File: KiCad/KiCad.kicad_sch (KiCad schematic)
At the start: 0 parts

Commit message: 提交初始BOM表
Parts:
- added U1: ESP32-WROOM-32E, RF_Module:ESP32-WROOM-32D, symbol RF_Module:ESP32-WROOM-32E
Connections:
- new net +3V3: U1.2 (VDD)
- new net GND: U1.1 (GND), U1.15 (GND), U1.38 (GND), U1.39 (GND)
- no-connect marks 0 -> 1

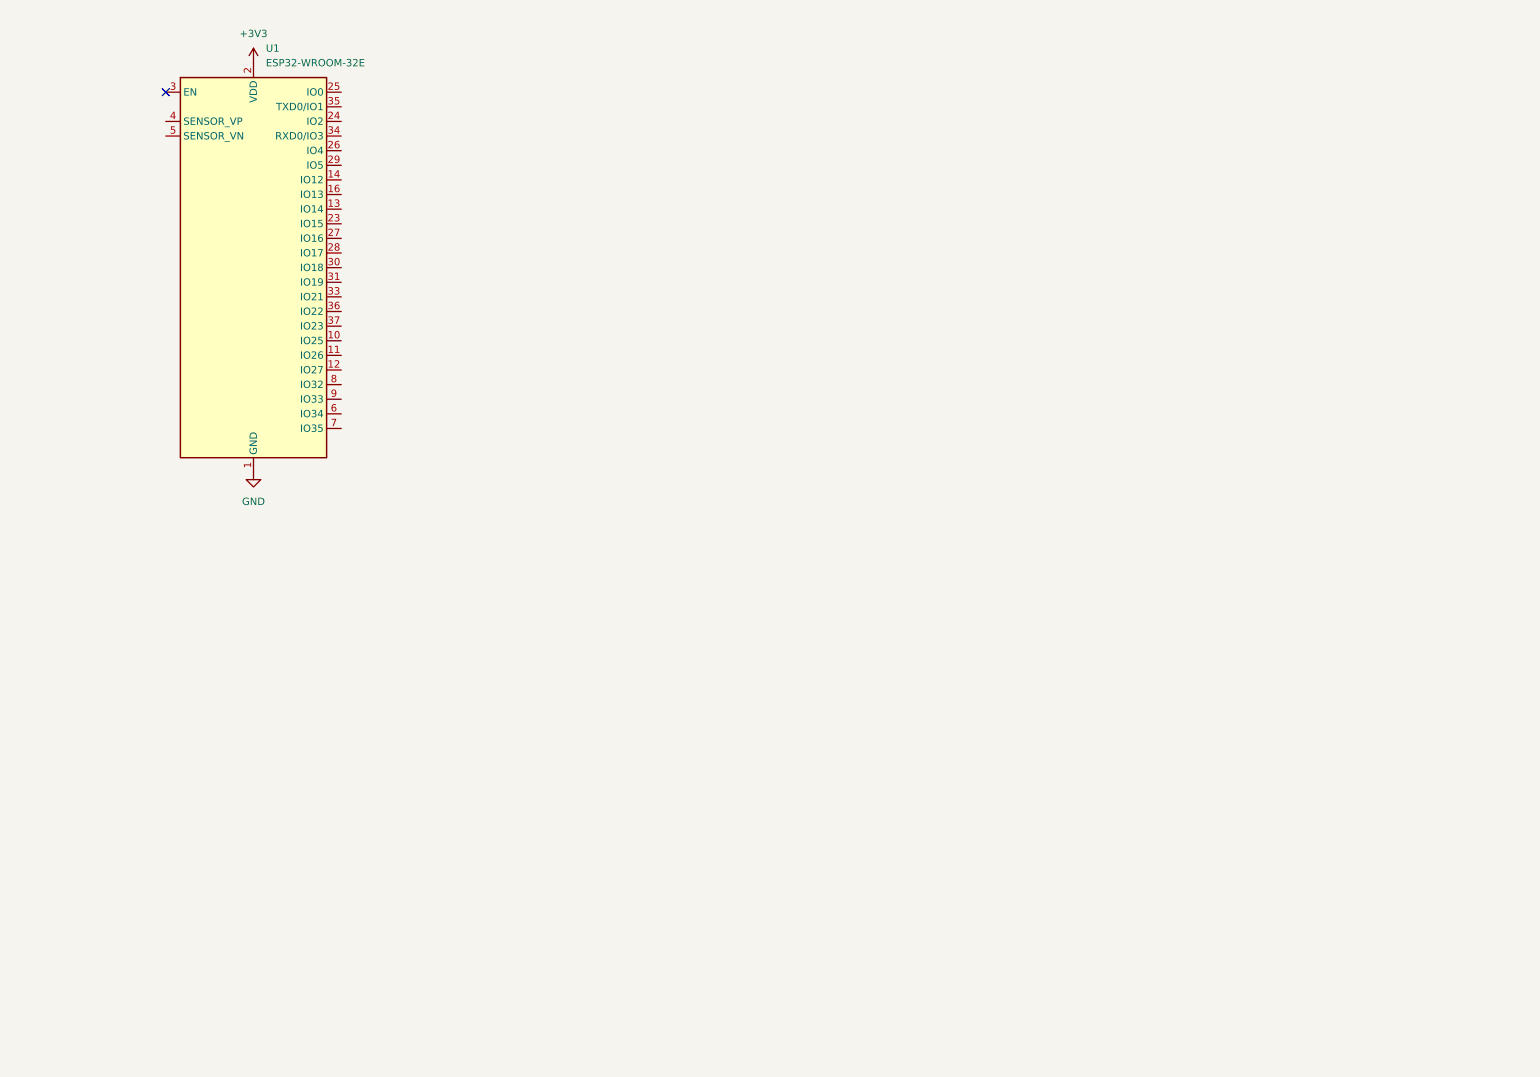
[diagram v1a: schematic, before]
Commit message: 完成主電源輸入轉到數位系統主電源軌電壓(12~24v to 5v)之原理圖，包含外部DC供電接口
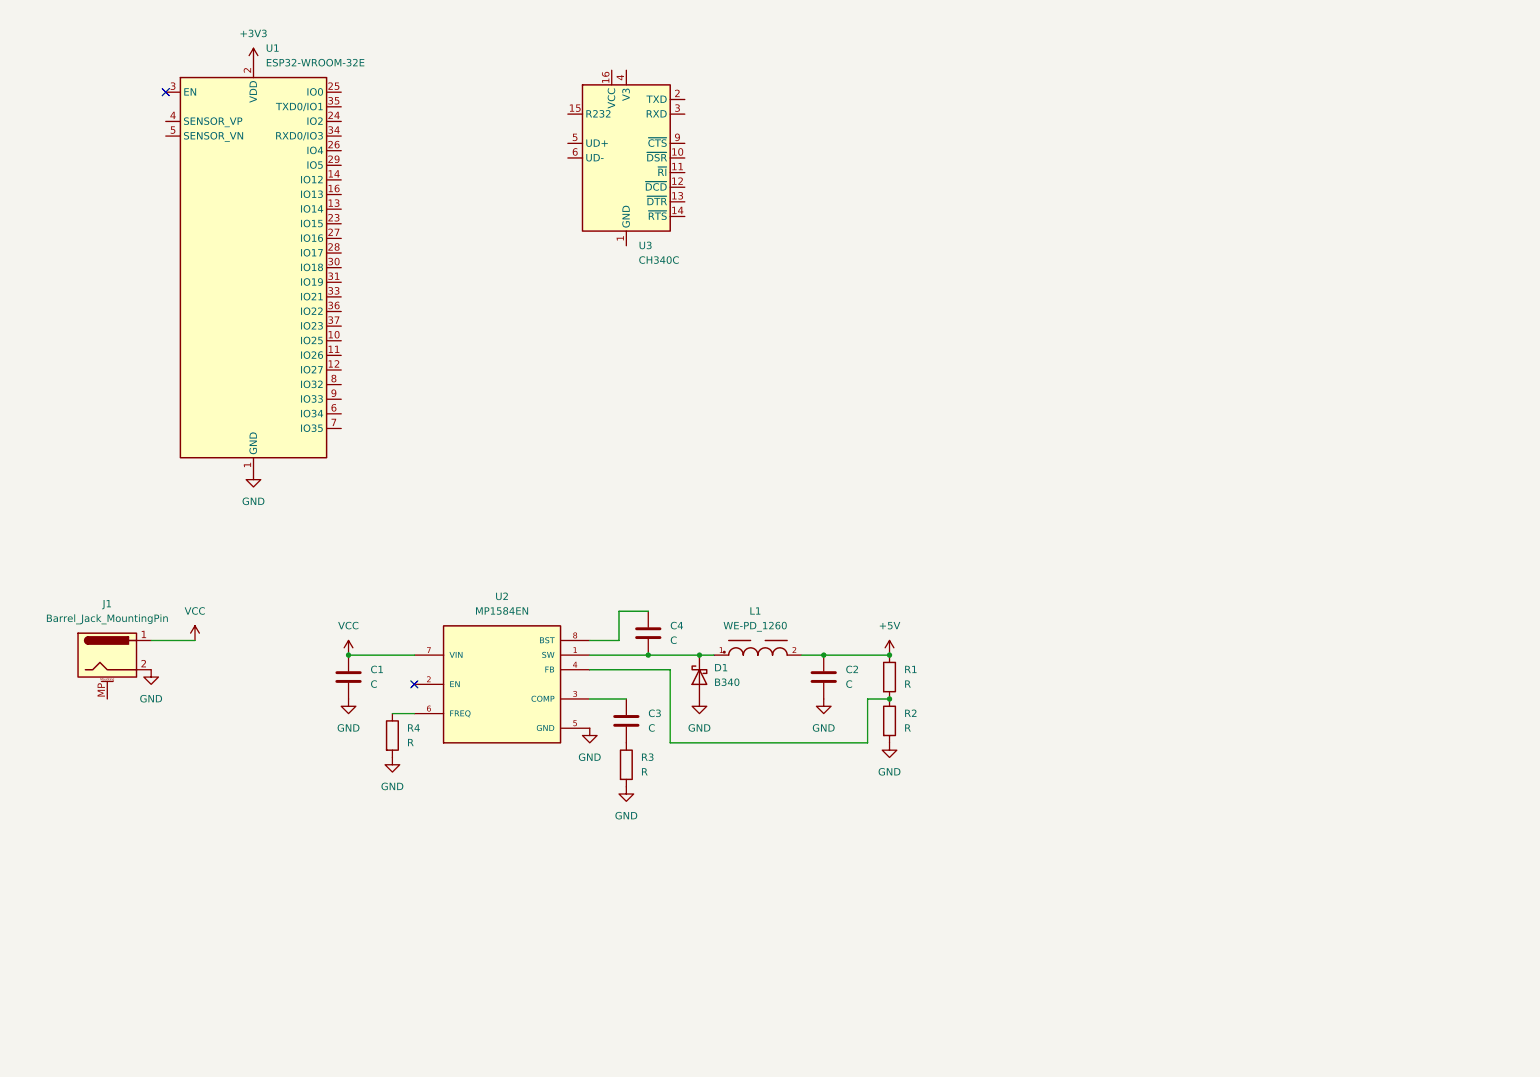
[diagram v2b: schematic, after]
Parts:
- added C1, C2, C3, C4: C, Capacitor_SMD:C_0603_1608Metric, symbol Device:C
- added D1: B340, Diode_SMD:D_SMC, symbol Diode:B340
- added J1: Barrel_Jack_MountingPin, Connector_BarrelJack:BarrelJack_Kycon_KLDX-0202-xC_Horizontal, symbol Connector:Barrel_Jack_MountingPin
- added L1: WE-PD_1260, DC-DC POWER L1:WE-PD_1260, symbol DC-DC POWER L1:WE-PD_1260
- added R1, R2, R4: R, Resistor_SMD:R_0603_1608Metric, symbol Device:R
- added R3: R, symbol Device:R
- added U2: MP1584EN, MP1584:SOIC127P600X170-9N, symbol MP1584:MP1584EN
- added U3: CH340C, Package_SO:SOIC-16_3.9x9.9mm_P1.27mm, symbol Interface_USB:CH340C
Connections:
- net GND: now also C1.2, C2.2, D1.2 (A), J1.2, R2.2, R3.2, R4.2, U2.5 (GND), U2.9 (GND)
- new net: R1.2, R2.1, U2.4 (FB)
- new net: C4.2, D1.1 (K), L1.1, U2.1 (SW)
- new net: C3.1, U2.3 (COMP)
- new net: R4.1, U2.6 (FREQ)
- new net: C4.1, U2.8 (BST)
- new net: C3.2, R3.1
- new net +5V: C2.1, L1.2, R1.1
- new net VCC: C1.1, J1.1, U2.7 (VIN)
- no-connect marks 1 -> 2

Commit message: 完成主電源輸入轉到數位系統主電源軌電壓模塊(12~24v to 5v)之PCB
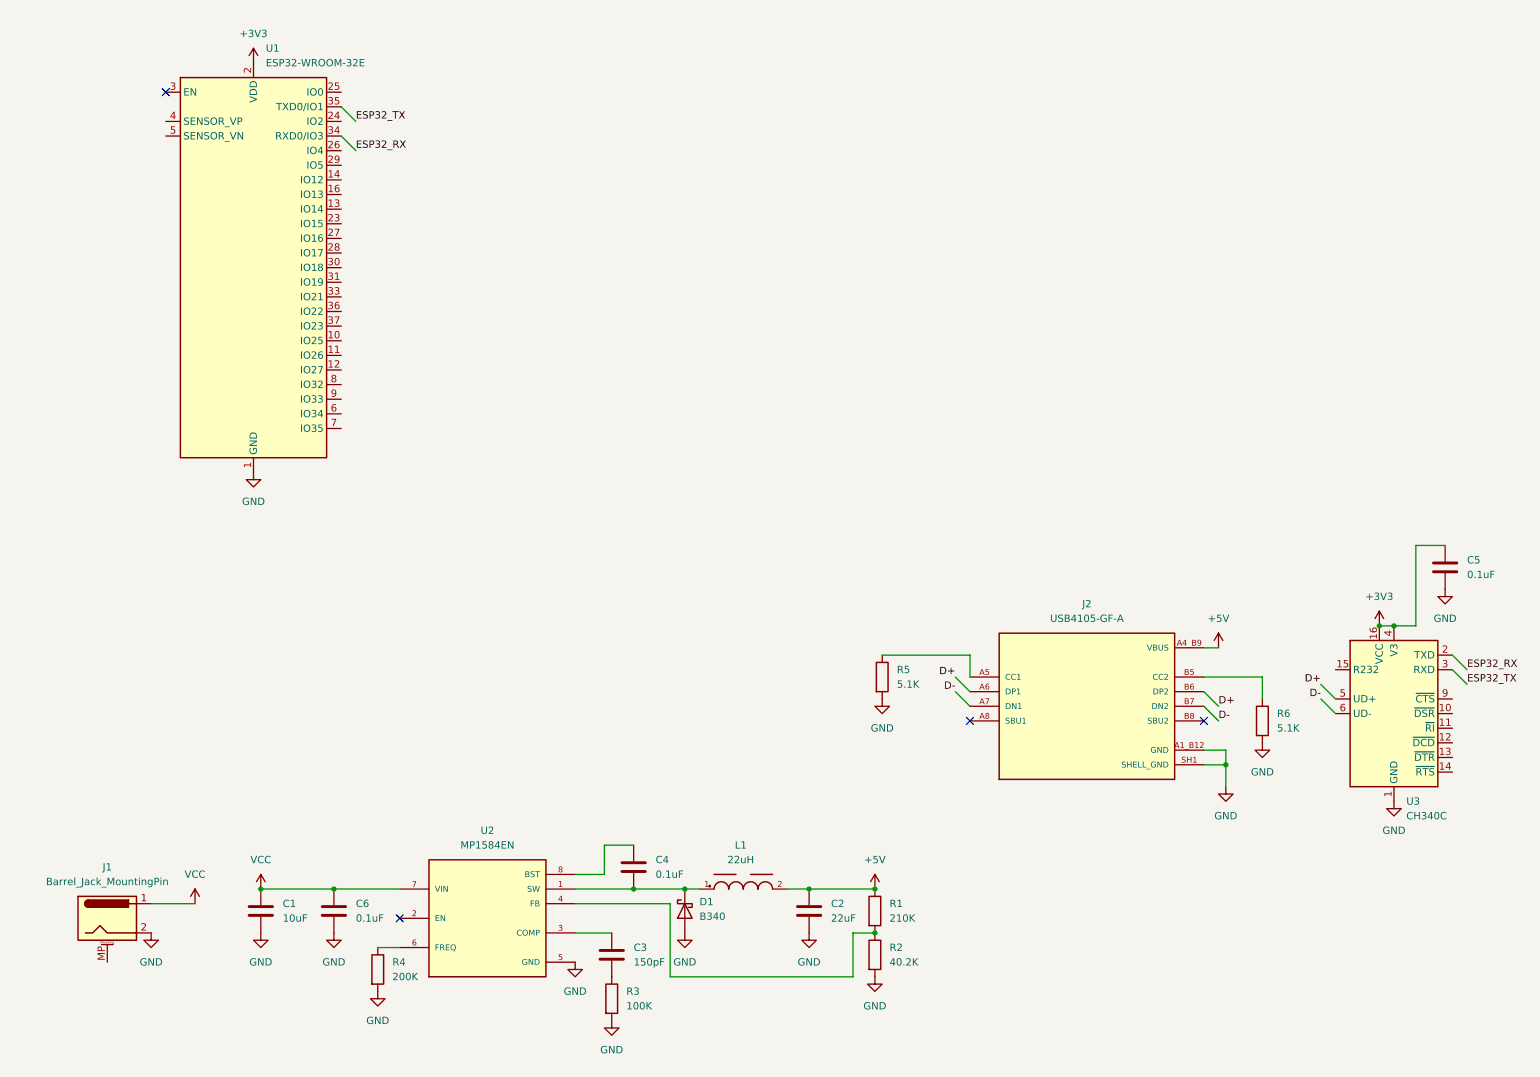
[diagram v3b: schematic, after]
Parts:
- added C5, C6: 0.1uF, Capacitor_SMD:C_0603_1608Metric, symbol Device:C
- added J2: USB4105-GF-A, USB4105-GF-A:GCT_USB4105-GF-A, symbol USB4105-GF-A:USB4105-GF-A
- added R5, R6: 5.1K, Resistor_SMD:R_0603_1608Metric, symbol Device:R
- C1: value C -> 10uF
- C2: value C -> 22uF; footprint Capacitor_SMD:C_0603_1608Metric -> Capacitor_SMD:C_0805_2012Metric
- C3: value C -> 150pF
- C4: value C -> 0.1uF
- L1: value WE-PD_1260 -> 22uH
- R1: value R -> 210K
- R2: value R -> 40.2K
- R3: value R -> 100K; footprint (none) -> Resistor_SMD:R_0603_1608Metric
- R4: value R -> 200K
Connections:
- net +3V3: now also U3.16 (VCC), U3.4 (V3), C5.1
- net +5V: now also J2.A4_B9 (VBUS), J2.B4_A9 (VBUS)
- net GND: now also U3.1 (GND), C5.2, C6.2, J2.A1_B12 (GND), J2.B1_A12 (GND), J2.SH1 (SHELL_GND), J2.SH2 (SHELL_GND), J2.SH3 (SHELL_GND), J2.SH4 (SHELL_GND), R5.2, R6.2
- net VCC: now also C6.1
- new net: J2.B5 (CC2), R6.1
- new net: J2.A5 (CC1), R5.1
- no-connect marks 2 -> 4
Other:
- moved on the sheet: C1, C3, C4, D1, J1, L1, R1, R2, R4, U2, U3

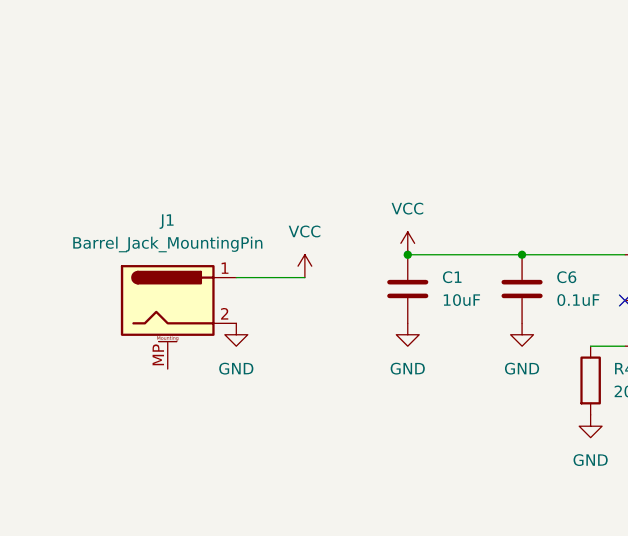
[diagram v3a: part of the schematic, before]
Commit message: 完成5v電源軌的所有電路
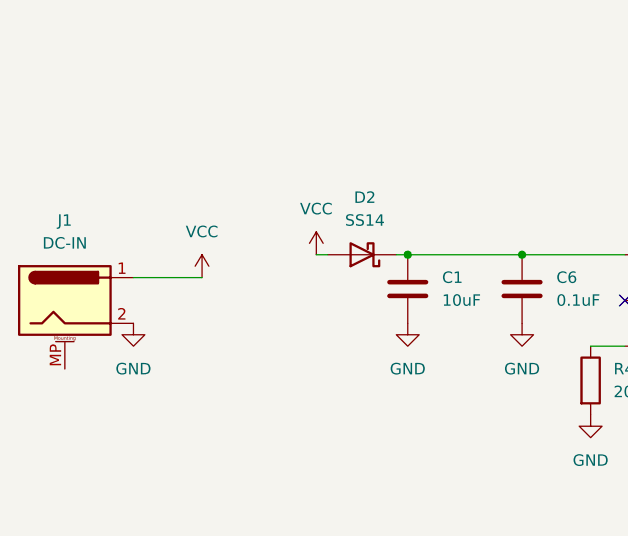
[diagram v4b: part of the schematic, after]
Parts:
- added D2: SS14, Diode_SMD:D_SMA, symbol Diode:SS14
- J1: value Barrel_Jack_MountingPin -> DC-IN
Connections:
- net VCC: now also D2.2 (A); no longer C1.1, C6.1, U2.7 (VIN)
- new net: C1.1, C6.1, D2.1 (K), U2.7 (VIN)
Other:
- moved on the sheet: J1
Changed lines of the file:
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@@
 	(wire
 		(pts
-			(xy 39.37 168.91) (xy 46.99 168.91)
+			(xy 27.94 168.91) (xy 35.56 168.91)
 		)
 		(stroke
@@
 		(pts
 			(xy 118.11 158.75) (xy 118.11 163.83)
+		)
+		(stroke
+			(width 0)
+			(type default)
+		)
+	)
+	(wire
+		(pts
+			(xy 57.15 166.37) (xy 58.42 166.37)
+		)
+		(stroke
+			(width 0)
+			(type default)
+		)
+	)
+	(wire
+		(pts
+			(xy 48.26 166.37) (xy 49.53 166.37)
 		)
 		(stroke
@@
 	(symbol
 		(lib_id "power:VCC")
-		(at 46.99 168.91 0)
+		(at 35.56 168.91 0)
 		(unit 1)
 		(exclude_from_sim no)
@@
 		(fields_autoplaced yes)
 		(property "Reference" "#PWR013"
-			(at 46.99 172.72 0)
+			(at 35.56 172.72 0)
 			(effects
 				(font
@@
 		)
 		(property "Value" "VCC"
-			(at 46.99 163.83 0)
+			(at 35.56 163.83 0)
 			(effects
 				(font
@@
 		)
 		(property "Footprint" ""
-			(at 46.99 168.91 0)
+			(at 35.56 168.91 0)
 			(effects
 				(font
@@
 		)
 		(property "Datasheet" ""
-			(at 46.99 168.91 0)
+			(at 35.56 168.91 0)
 			(effects
 				(font
@@
 		)
 		(property "Description" "Power symbol creates a global label with name \"VCC\""
-			(at 46.99 168.91 0)
+			(at 35.56 168.91 0)
 			(effects
 				(font
@@
 				(path "/8145d5a2-4aff-47fb-b6a2-0059c8017b6c"
 					(reference "#PWR013")
+					(unit 1)
+				)
+			)
+		)
+	)
+	(symbol
+		(lib_id "Diode:SS14")
+		(at 53.34 166.37 180)
+		(unit 1)
+		(exclude_from_sim no)
+		(in_bom yes)
+		(on_board yes)
+		(dnp no)
+		(fields_autoplaced yes)
+		(property "Reference" "D2"
+			(at 53.6575 160.02 0)
+			(effects
+				(font
+					(size 1.27 1.27)
+				)
+			)
+		)
+		(property "Value" "SS14"
+			(at 53.6575 162.56 0)
+			(effects
+				(font
+					(size 1.27 1.27)
+				)
+			)
+		)
+		(property "Footprint" "Diode_SMD:D_SMA"
+			(at 53.34 161.925 0)
+			(effects
+				(font
+					(size 1.27 1.27)
+				)
+				(hide yes)
+			)
+		)
+		(property "Datasheet" "https://www.vishay.com/docs/88746/ss12.pdf"
+			(at 53.34 166.37 0)
+			(effects
+				(font
+					(size 1.27 1.27)
+				)
+				(hide yes)
+			)
+		)
+		(property "Description" "40V 1A Schottky Diode, SMA"
+			(at 53.34 166.37 0)
+			(effects
+				(font
+					(size 1.27 1.27)
+				)
+				(hide yes)
+			)
+		)
+		(pin "2"
+		)
+		(pin "1"
+		)
+		(instances
+			(project ""
+				(path "/8145d5a2-4aff-47fb-b6a2-0059c8017b6c"
+					(reference "D2")
 					(unit 1)
 				)
@@
 	(symbol
 		(lib_id "power:GND")
-		(at 39.37 173.99 0)
+		(at 27.94 173.99 0)
 		(unit 1)
 		(exclude_from_sim no)
@@
 		(fields_autoplaced yes)
 		(property "Reference" "#PWR04"
-			(at 39.37 180.34 0)
+			(at 27.94 180.34 0)
 			(effects
 				(font
@@
 		)
 		(property "Value" "GND"
-			(at 39.37 179.07 0)
+			(at 27.94 179.07 0)
 			(effects
 				(font
@@
 		)
 		(property "Footprint" ""
-			(at 39.37 173.99 0)
+			(at 27.94 173.99 0)
 			(effects
 				(font
@@
 		)
 		(property "Datasheet" ""
-			(at 39.37 173.99 0)
+			(at 27.94 173.99 0)
 			(effects
 				(font
@@
 		)
 		(property "Description" "Power symbol creates a global label with name \"GND\" , ground"
-			(at 39.37 173.99 0)
+			(at 27.94 173.99 0)
 			(effects
 				(font
@@
 	(symbol
 		(lib_id "Connector:Barrel_Jack_MountingPin")
-		(at 31.75 171.45 0)
+		(at 20.32 171.45 0)
 		(unit 1)
 		(exclude_from_sim no)
@@
 		(fields_autoplaced yes)
 		(property "Reference" "J1"
-			(at 31.75 162.56 0)
-			(effects
-				(font
-					(size 1.27 1.27)
-				)
-			)
-		)
-		(property "Value" "Barrel_Jack_MountingPin"
-			(at 31.75 165.1 0)
+			(at 20.32 162.56 0)
+			(effects
+				(font
+					(size 1.27 1.27)
+				)
+			)
+		)
+		(property "Value" "DC-IN"
+			(at 20.32 165.1 0)
 			(effects
 				(font
@@
 		)
 		(property "Footprint" "Connector_BarrelJack:BarrelJack_Kycon_KLDX-0202-xC_Horizontal"
-			(at 33.02 172.466 0)
+			(at 21.59 172.466 0)
 			(effects
 				(font
@@
 		)
 		(property "Datasheet" "~"
-			(at 33.02 172.466 0)
+			(at 21.59 172.466 0)
 			(effects
 				(font
@@
 		)
 		(property "Description" "DC Barrel Jack with a mounting pin"
-			(at 31.75 171.45 0)
+			(at 20.32 171.45 0)
 			(effects
 				(font
@@
 	(symbol
 		(lib_id "power:VCC")
-		(at 58.42 166.37 0)
+		(at 48.26 166.37 0)
 		(unit 1)
 		(exclude_from_sim no)
@@
 		(fields_autoplaced yes)
 		(property "Reference" "#PWR014"
-			(at 58.42 170.18 0)
+			(at 48.26 170.18 0)
 			(effects
 				(font
@@
 		)
 		(property "Value" "VCC"
-			(at 58.42 161.29 0)
+			(at 48.26 161.29 0)
 			(effects
 				(font
@@
 		)
 		(property "Footprint" ""
-			(at 58.42 166.37 0)
+			(at 48.26 166.37 0)
 			(effects
 				(font
@@
 		)
 		(property "Datasheet" ""
-			(at 58.42 166.37 0)
+			(at 48.26 166.37 0)
 			(effects
 				(font
@@
 		)
 		(property "Description" "Power symbol creates a global label with name \"VCC\""
-			(at 58.42 166.37 0)
-			(effects
-				(font
+			(at 48.26 166.37 0)
+			(effects
+				(font
